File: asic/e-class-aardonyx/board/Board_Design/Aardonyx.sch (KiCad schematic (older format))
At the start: 8 parts

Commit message: updated the component
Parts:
- H1, H2, H3, H4, H5, H6: footprint MountingHole:MountingHole_3.5mm_Pad_Via -> MountingHole:MountingHole_3.2mm_M3
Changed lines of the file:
@@
 F 0 "H5" H 2550 6696 50  0000 L CNN
 F 1 "MountingHole" H 2550 6605 50  0000 L CNN
-F 2 "MountingHole:MountingHole_3.5mm_Pad_Via" H 2450 6650 50  0001 C CNN
+F 2 "MountingHole:MountingHole_3.2mm_M3" H 2450 6650 50  0001 C CNN
 F 3 "~" H 2450 6650 50  0001 C CNN
 	1    2450 6650
@@
 F 0 "H6" H 2550 7246 50  0000 L CNN
 F 1 "MountingHole" H 2550 7155 50  0000 L CNN
-F 2 "MountingHole:MountingHole_3.5mm_Pad_Via" H 2450 7200 50  0001 C CNN
+F 2 "MountingHole:MountingHole_3.2mm_M3" H 2450 7200 50  0001 C CNN
 F 3 "~" H 2450 7200 50  0001 C CNN
 	1    2450 7200
@@
 F 0 "H3" H 1750 6696 50  0000 L CNN
 F 1 "MountingHole" H 1750 6605 50  0000 L CNN
-F 2 "MountingHole:MountingHole_3.5mm_Pad_Via" H 1650 6650 50  0001 C CNN
+F 2 "MountingHole:MountingHole_3.2mm_M3" H 1650 6650 50  0001 C CNN
 F 3 "~" H 1650 6650 50  0001 C CNN
 	1    1650 6650
@@
 F 0 "H4" H 1750 7246 50  0000 L CNN
 F 1 "MountingHole" H 1750 7155 50  0000 L CNN
-F 2 "MountingHole:MountingHole_3.5mm_Pad_Via" H 1650 7200 50  0001 C CNN
+F 2 "MountingHole:MountingHole_3.2mm_M3" H 1650 7200 50  0001 C CNN
 F 3 "~" H 1650 7200 50  0001 C CNN
 	1    1650 7200
@@
 F 0 "H2" H 900 7246 50  0000 L CNN
 F 1 "MountingHole" H 900 7155 50  0000 L CNN
-F 2 "MountingHole:MountingHole_3.5mm_Pad_Via" H 800 7200 50  0001 C CNN
+F 2 "MountingHole:MountingHole_3.2mm_M3" H 800 7200 50  0001 C CNN
 F 3 "~" H 800 7200 50  0001 C CNN
 	1    800  7200
@@
 F 0 "H1" H 900 6696 50  0000 L CNN
 F 1 "MountingHole" H 900 6605 50  0000 L CNN
-F 2 "MountingHole:MountingHole_3.5mm_Pad_Via" H 800 6650 50  0001 C CNN
+F 2 "MountingHole:MountingHole_3.2mm_M3" H 800 6650 50  0001 C CNN
 F 3 "~" H 800 6650 50  0001 C CNN
 	1    800  6650

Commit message: Added few components
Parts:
- added H7: MountingHole, MountingHole:MountingHole_3.2mm_M3, symbol Mechanical:MountingHole
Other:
- moved on the sheet: FID1, FID2
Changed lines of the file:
@@
 F14 "I2C0_SCL" B R 4350 2900 50
 F15 "I2C0_SDA" B R 4350 3000 50
-F16 "SPI1_nCS" I R 4350 5000 50
-F17 "SPI1_CLK" I R 4350 5100 50
+F16 "SPI1_nCS" I R 4350 5100 50
+F17 "SPI1_CLK" I R 4350 5000 50
 F18 "SPI1_MISO" O R 4350 5200 50
 F19 "SPI1_MOSI" I R 4350 5300 50
@@
 L Mechanical:Fiducial FID2
 U 1 1 5EE1DA72
-P 3450 7250
-F 0 "FID2" H 3535 7296 50  0000 L CNN
-F 1 "Fiducial" H 3535 7205 50  0000 L CNN
-F 2 "Fiducial:Fiducial_1.5mm_Mask3mm" H 3450 7250 50  0001 C CNN
-F 3 "~" H 3450 7250 50  0001 C CNN
-	1    3450 7250
+P 4150 7150
+F 0 "FID2" H 4235 7196 50  0000 L CNN
+F 1 "Fiducial" H 4235 7105 50  0000 L CNN
+F 2 "Fiducial:Fiducial_1.5mm_Mask3mm" H 4150 7150 50  0001 C CNN
+F 3 "~" H 4150 7150 50  0001 C CNN
+	1    4150 7150
 	1    0    0    -1
 $EndComp
@@
 L Mechanical:Fiducial FID1
 U 1 1 5EE1DFF3
-P 3450 6750
-F 0 "FID1" H 3535 6796 50  0000 L CNN
-F 1 "Fiducial" H 3535 6705 50  0000 L CNN
-F 2 "Fiducial:Fiducial_1.5mm_Mask3mm" H 3450 6750 50  0001 C CNN
-F 3 "~" H 3450 6750 50  0001 C CNN
-	1    3450 6750
+P 4150 6650
+F 0 "FID1" H 4235 6696 50  0000 L CNN
+F 1 "Fiducial" H 4235 6605 50  0000 L CNN
+F 2 "Fiducial:Fiducial_1.5mm_Mask3mm" H 4150 6650 50  0001 C CNN
+F 3 "~" H 4150 6650 50  0001 C CNN
+	1    4150 6650
 	1    0    0    -1
 $EndComp
@@
 	1    0    0    -1
 $EndComp
+$Comp
+L Mechanical:MountingHole H7
+U 1 1 5EEDD3DD
+P 3250 6650
+F 0 "H7" H 3350 6696 50  0000 L CNN
+F 1 "MountingHole" H 3350 6605 50  0000 L CNN
+F 2 "MountingHole:MountingHole_3.2mm_M3" H 3250 6650 50  0001 C CNN
+F 3 "~" H 3250 6650 50  0001 C CNN
+	1    3250 6650
+	1    0    0    -1
+$EndComp

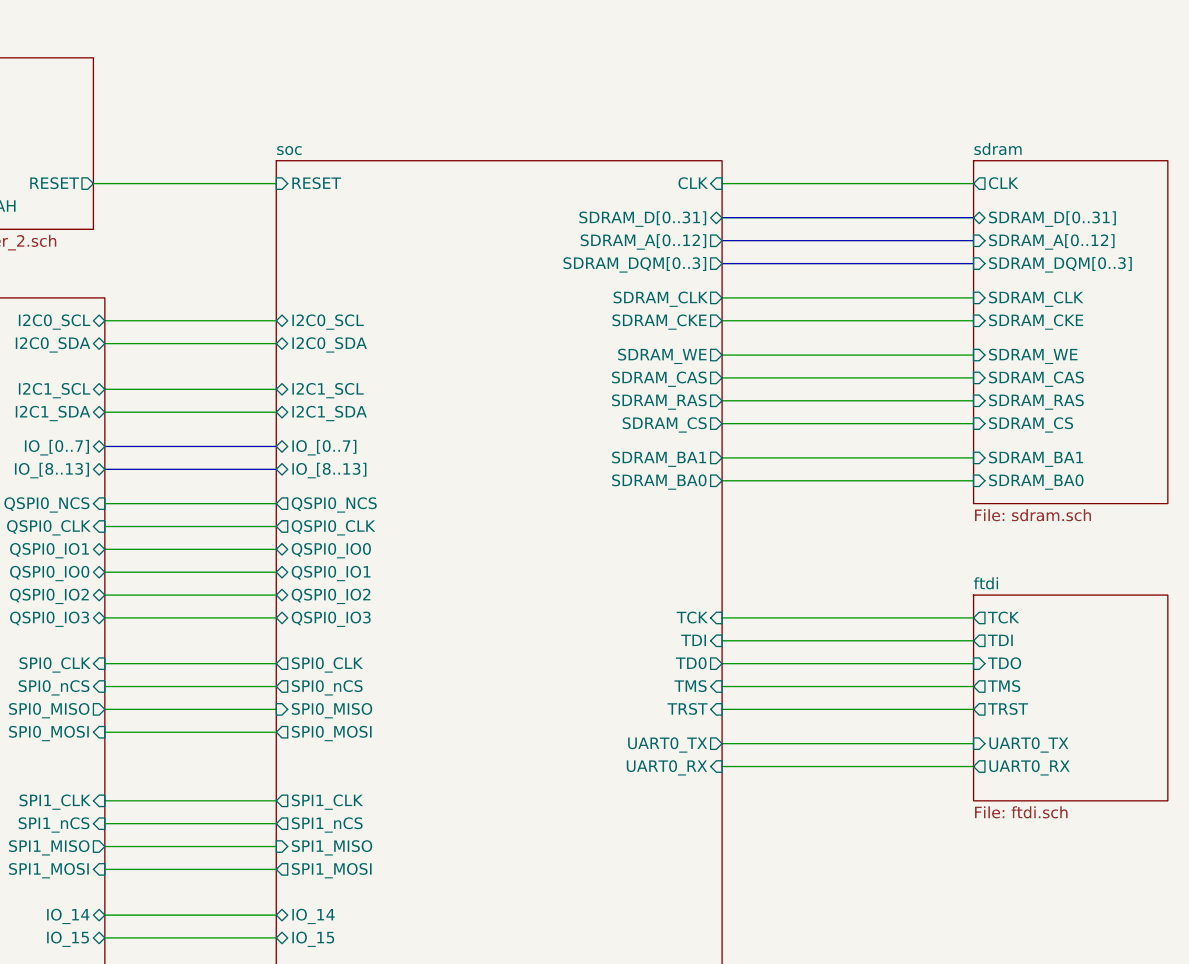
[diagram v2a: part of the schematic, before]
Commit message: Replacing ADM1085 with ADM1186
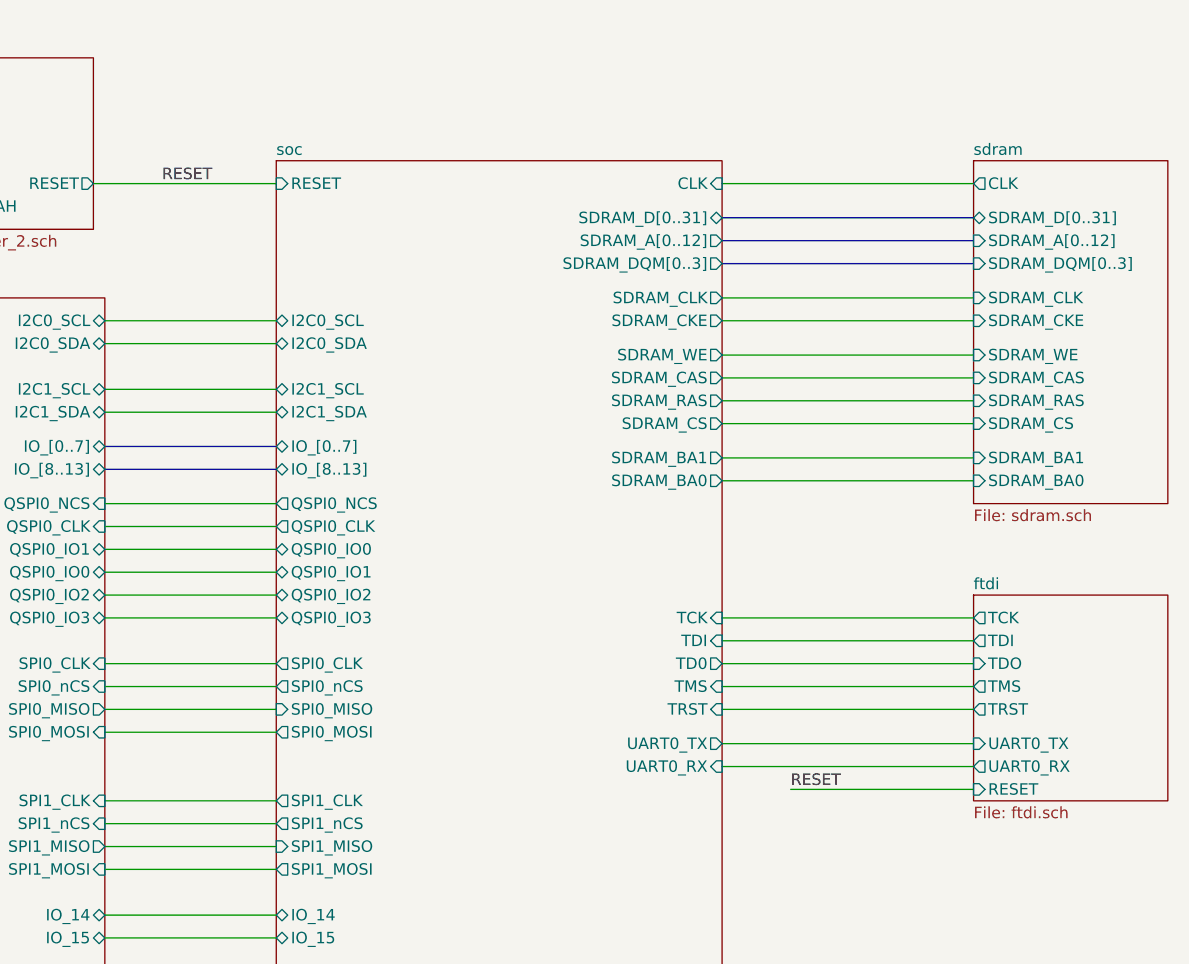
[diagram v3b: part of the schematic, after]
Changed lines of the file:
@@
 F7 "UART0_RX" O L 8150 4850 50
 F8 "UART0_TX" I L 8150 4750 50
+F9 "RESET" I L 8150 4950 50
 $EndSheet
 $Sheet
@@
 	1    0    0    -1
 $EndComp
+Text Label 4600 2300 0    50   ~ 0
+RESET
+Wire Wire Line
+	7350 4950 8150 4950
+Text Label 7350 4950 0    50   ~ 0
+RESET
 $EndSCHEMATC
